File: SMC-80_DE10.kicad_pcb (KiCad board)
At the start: 4 copper layers, 63.5 x 58.9 mm, 27 parts, among them J1 Arduino1, J2 Arduino2, J3 DE10-Lite GPIO, J4 Port A, U1 Z84C0010AEG, U2 Z84C4310AEG, U3 SST39LF040, U4 AS6C4008A-55ZIN

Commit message: added SIO port B clock
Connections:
- J1 pad 1: (no net) -> Net-(J1-Pad1)
- J1 pad 2: (no net) -> Net-(J1-Pad2)
- J1 pad 3: (no net) -> Net-(J1-Pad3)
- J2 pad 5: (no net) -> Net-(J2-Pad5)
- J2 pad 6: (no net) -> Net-(J2-Pad6)
- J2 pad 7: (no net) -> Net-(J2-Pad7)
- J2 pad 8: (no net) -> Net-(J2-Pad8)
- J3 pad 1: (no net) -> Net-(J3-Pad1)
- J3 pad 11: (no net) -> +5V
- J3 pad 3: (no net) -> Net-(J3-Pad3)
- J3 pad 37: (no net) -> Net-(J3-Pad37)
- J3 pad 38: (no net) -> Net-(J3-Pad38)
- J4 pad 3: (no net) -> Net-(J4-Pad3)
- U1 pad 11: (no net) -> Net-(U1-Pad11)
- U1 pad 17: (no net) -> Net-(U1-Pad17)
- U1 pad 20: (no net) -> Net-(U1-Pad20)
- U1 pad 25: (no net) -> Net-(U1-Pad25)
- U1 pad 33: (no net) -> Net-(U1-Pad33)
- U1 pad 39: (no net) -> Net-(U1-Pad39)
- U2 pad 1: (no net) -> Net-(U2-Pad1)
- U2 pad 10: (no net) -> Net-(U2-Pad10)
- U2 pad 11: (no net) -> Net-(U2-Pad11)
- U2 pad 12: (no net) -> /CLK_U
- U2 pad 13: (no net) -> /CLK_U
- U2 pad 14: (no net) -> Net-(U2-Pad14)
- U2 pad 15: (no net) -> Net-(U2-Pad15)
- U2 pad 16: (no net) -> Net-(U2-Pad16)
- U2 pad 17: (no net) -> Net-(U2-Pad17)
- U2 pad 28: (no net) -> Net-(U2-Pad28)
- U2 pad 35: (no net) -> Net-(U2-Pad35)
- U2 pad 38: (no net) -> Net-(U2-Pad38)
- U2 pad 39: (no net) -> Net-(U2-Pad39)
- U2 pad 40: (no net) -> Net-(U2-Pad40)
- U2 pad 8: (no net) -> Net-(U2-Pad8)
- U2 pad 9: (no net) -> Net-(U2-Pad9)
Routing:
- net /CLK_U: track 58.2 -> 72.1 mm, vias 2 -> 3

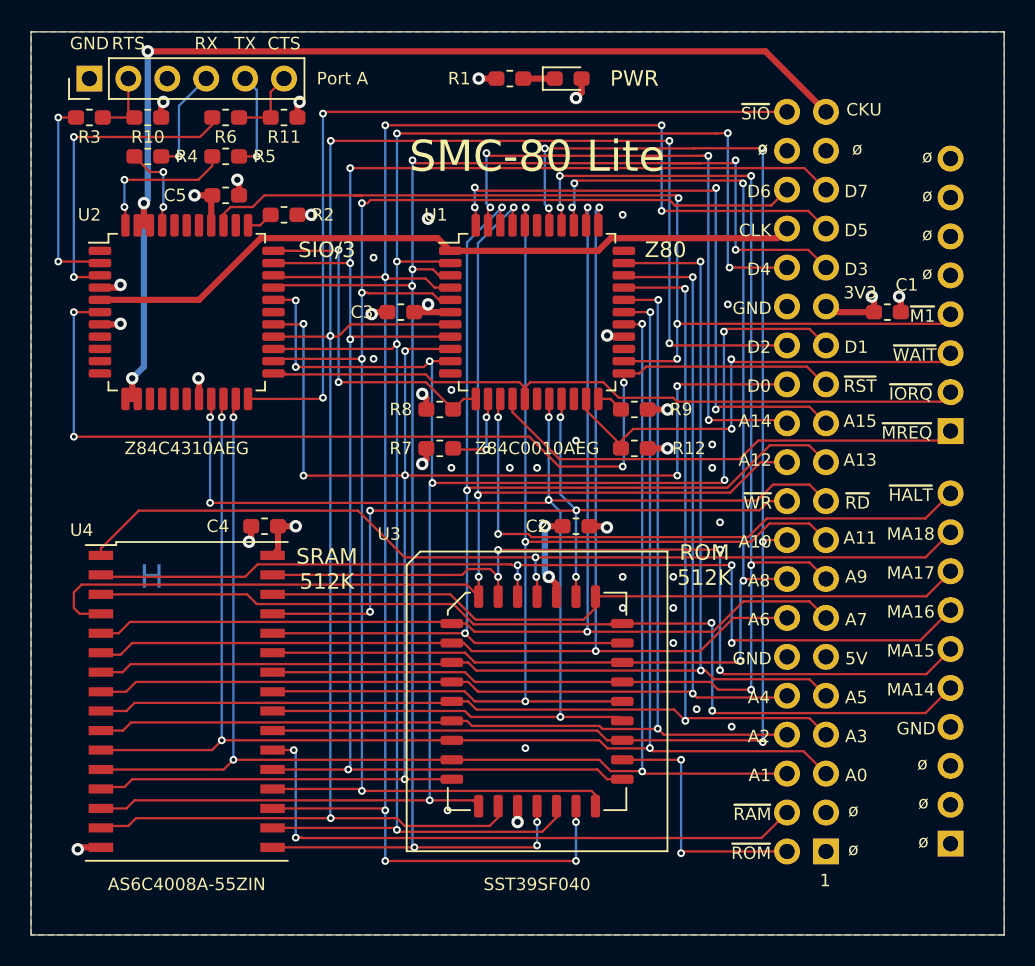
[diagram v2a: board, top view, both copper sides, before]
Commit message: Broke out SIO C/D and B/A pins
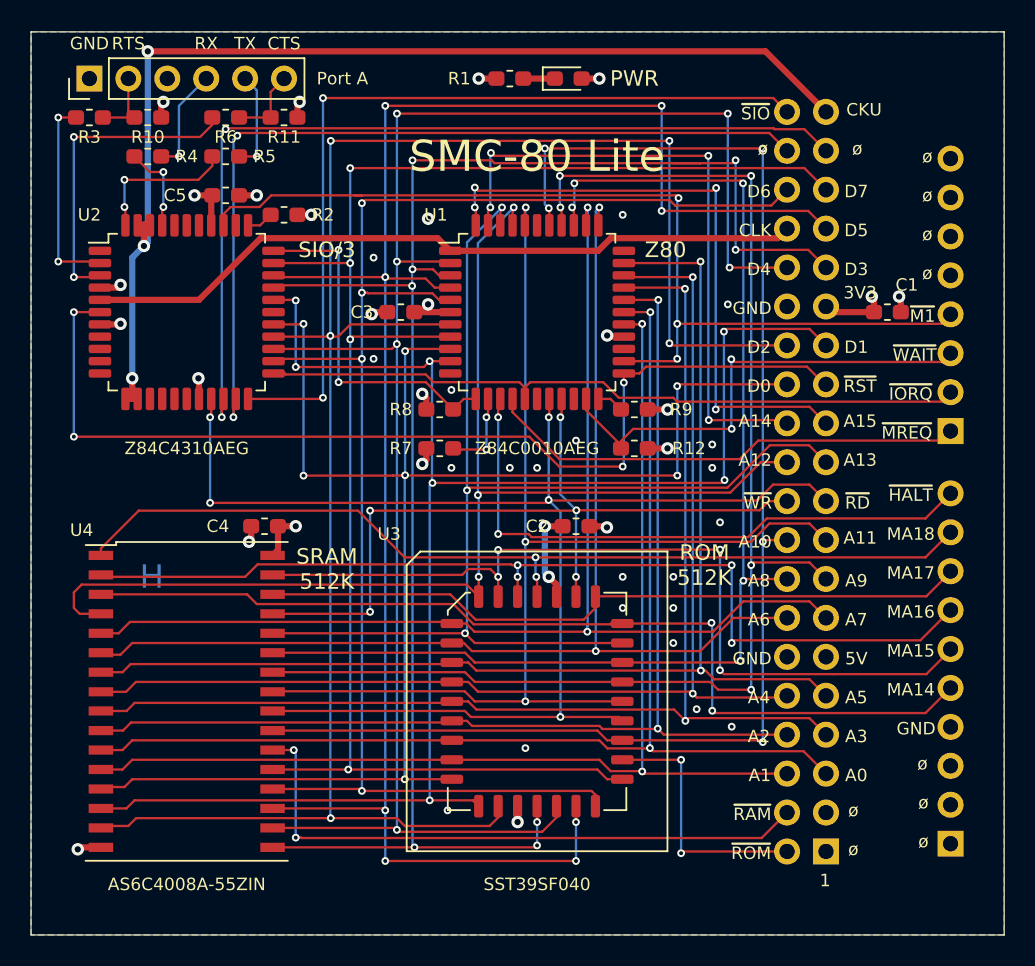
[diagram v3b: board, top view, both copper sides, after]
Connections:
- J3 pad 37: Net-(J3-Pad37) -> /C~D
- J3 pad 38: Net-(J3-Pad38) -> /B~A
- U2 pad 20: /A1 -> /C~D
- U2 pad 21: /A0 -> /B~A
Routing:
- net /C~D: track 0.00 -> 59.9 mm, vias 0 -> 2
- net /B~A: track 0.00 -> 56.2 mm, vias 0 -> 2
- net /A0: track 99.4 -> 75.8 mm, vias 4 -> 2
- net /A1: track 101.0 -> 78.7 mm, vias 4 -> 2
- net /D4: track 111.1 -> 113.6 mm
- net /D5: track 118.1 -> 120.7 mm
- net /A14: track 44.1 -> 42.3 mm
- net /SIO_~CE: track 54.1 -> 55.2 mm
- net Net-(J4-Pad2): track 5.32 -> 4.76 mm

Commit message: Add bottom silkscreens for FPGA pins
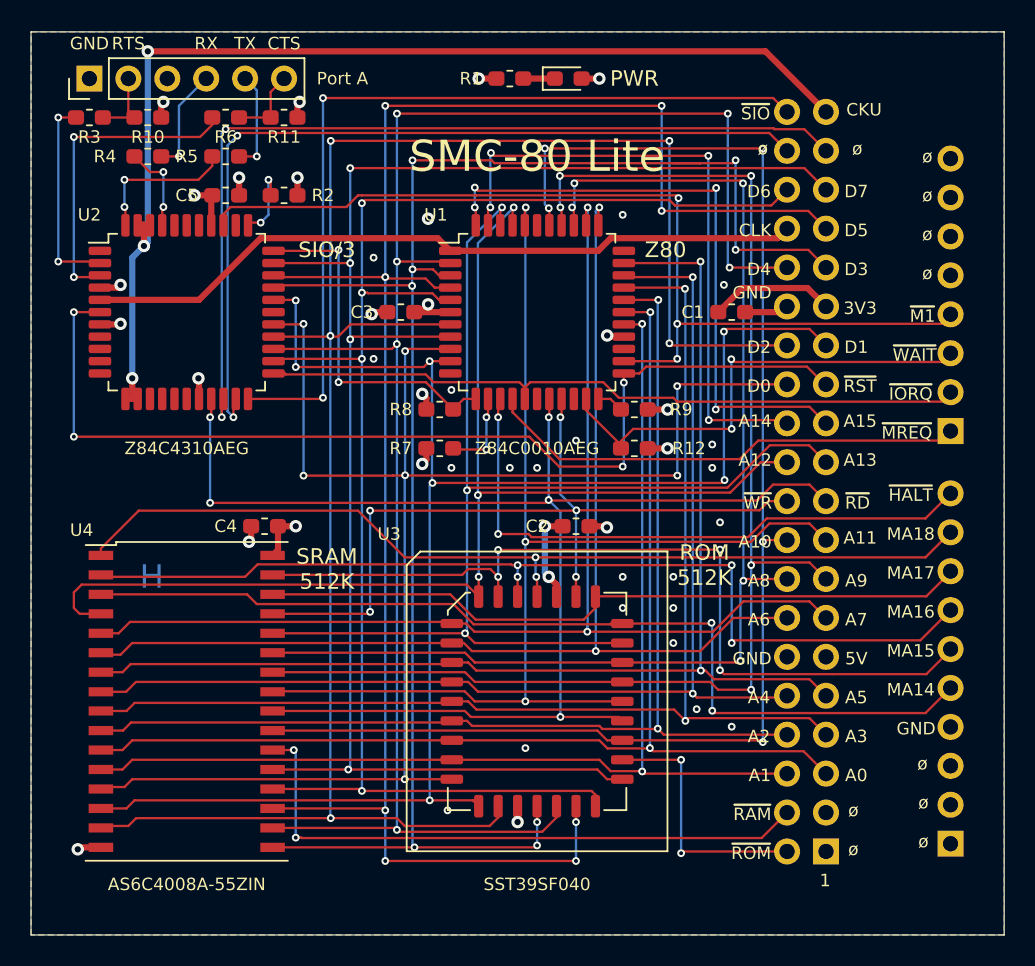
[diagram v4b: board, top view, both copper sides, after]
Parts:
- moved C1 10.2 mm to (146.1, 87.6)
- moved G*** 5.34 mm to (120.4, 101.1)
- moved R2 1.27 mm to (116.8, 80.0)
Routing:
- net VCC: track 28.2 -> 32.8 mm, vias 13 -> 12
- net Net-(R2-Pad2): track 1.76 -> 4.98 mm, vias 0 -> 2
- net GND: track 15.6 -> 17.5 mm, vias 35 -> 34
- net /~M1: track 63.5 -> 63.0 mm
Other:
- board text added: "AA10"
- board text added: "AA11"
- board text added: "AA12"
- board text added: "AA14"
- board text added: "AA15"
- board text added: "AA17"
- board text added: "AA19"
- board text added: "AA2"
- board text added: "AA5"
- board text added: "AA6"
- board text added: "AA7"
- board text added: "AA8"
- board text added: "AA9"
- board text added: "AB10"
- board text added: "AB11"
- board text added: "AB12"
- board text added: "AB13"
- board text added: "AB17"
- board text added: "AB19"
- board text added: "AB2"
- board text added: "AB20"
- board text added: "AB3"
- board text added: "AB9"
- board text added: "V5"
- board text added: "V7"
- board text added: "V8"
- board text added: "W10"
- board text added: "W11"
- board text added: "W12"
- board text added: "W13"
- board text added: "W5"
- board text added: "W6"
- board text added: "W7"
- board text added: "W8"
- board text added: "W9"
- board text added: "Y10"
- board text added: "Y11"
- board text added: "Y19"
- board text added: "Y3"
- board text added: "Y4"
- board text added: "Y5"
- board text added: "Y6"
- board text added: "Y7"
- board text added: "Y8"

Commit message: extra space for z80 pullups
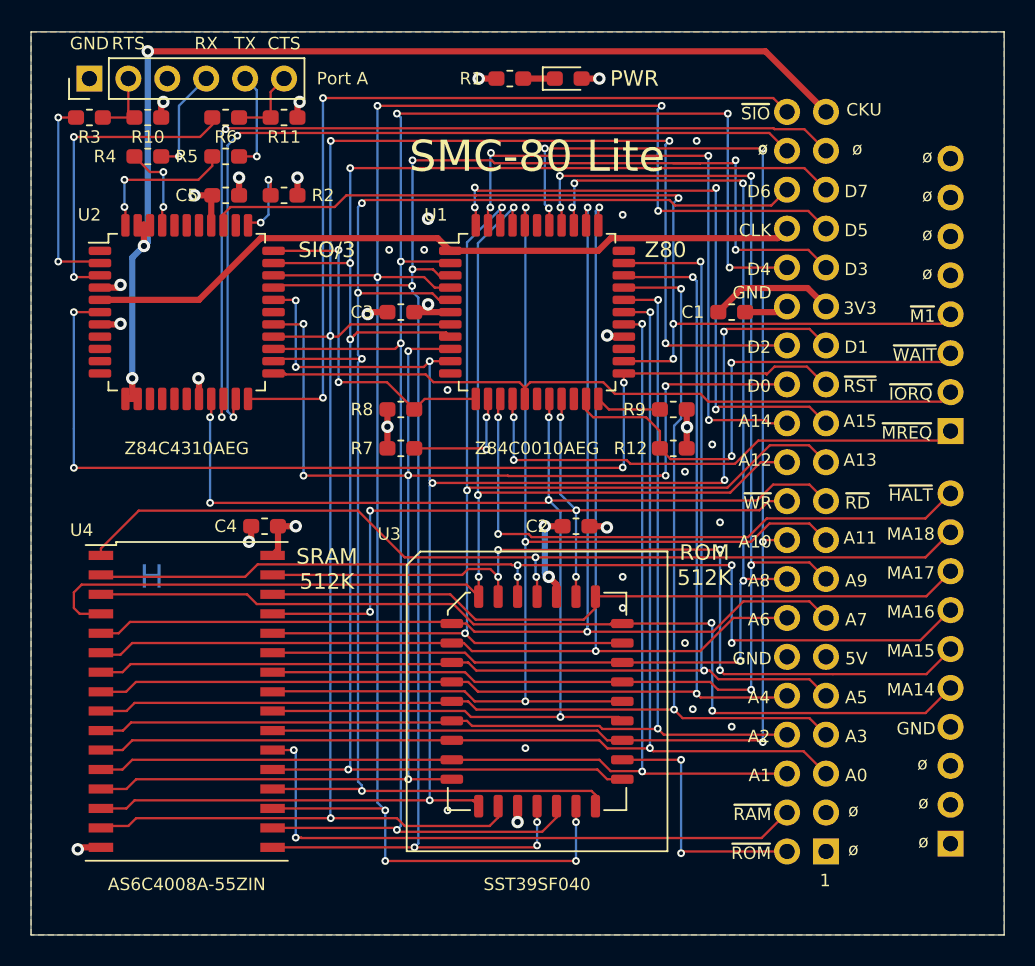
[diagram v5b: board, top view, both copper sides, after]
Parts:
- moved R12 2.54 mm to (142.2, 96.5)
- moved R9 2.54 mm to (142.2, 94.0)
- moved R7 2.54 mm to (124.5, 96.5)
- moved R8 2.54 mm to (124.5, 94.0)
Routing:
- net /Ram Rom and CPU/~BUSRQ: track 1.76 -> 4.30 mm
- net /Ram Rom and CPU/~NMI: track 5.55 -> 8.09 mm
- net /~MREQ: track 31.7 -> 33.8 mm, vias 0 -> 2
- net /~WAIT: track 31.4 -> 33.0 mm
- net /~RESET: track 66.4 -> 67.8 mm
- net /D5: track 120.7 -> 121.7 mm
- net /A3: track 80.8 -> 79.9 mm
- net /D6: track 100.5 -> 101.2 mm
- net VCC: track 32.8 -> 33.1 mm, vias 12 -> 10
- net GND: track 17.5 -> 17.7 mm, vias 34 -> 28

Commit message: smoothed traces
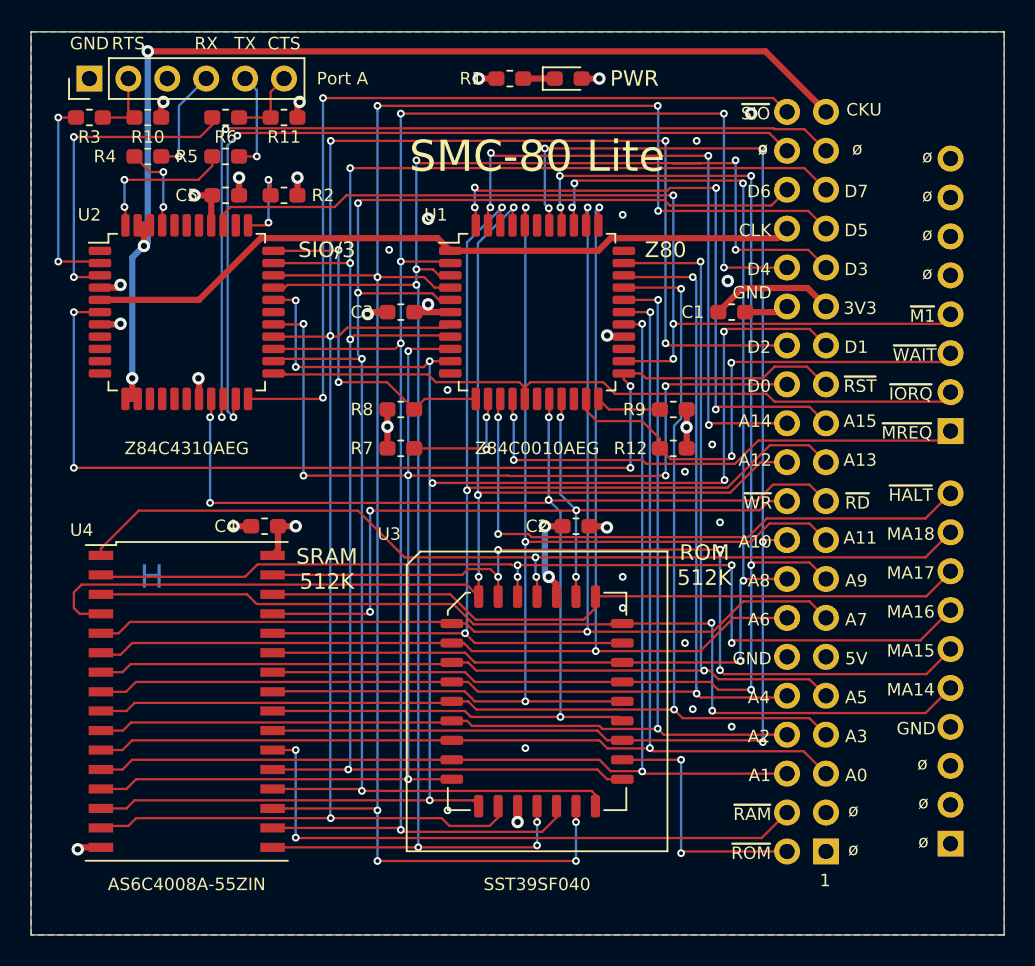
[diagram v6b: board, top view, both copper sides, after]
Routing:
- net /~RESET: track 67.8 -> 68.6 mm
- net /D5: track 121.7 -> 121.2 mm
- net GND: track 17.7 -> 17.8 mm, vias 28 -> 29
